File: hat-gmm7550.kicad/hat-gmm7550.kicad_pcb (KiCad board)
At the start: 4 copper layers, 65 x 56 mm, 83 parts, among them J1 VisionFive_GPIO, J10 Pmod 2x6, J2 Conn_01x02, J3 Conn_02x02_Odd_Even, J4 DNI, J5 DNI, J6 10144517-064802LF, J7 10144517-064802LF, J8 JTAG, J9 Pmod 2x6, Q1 NX6008NBK, Q2 NX6008NBK, Q3 NX6008NBK, Q4 FDC855N, U1 CAT24C32Y, U2 74LVC1G07, U3 ADM1177, U4 LSF0204PW, U5 LSF0204PW, U6 LSF0204PW, U7 LSF0204PW, U8 LSF0204PW, U9 LSF0204PW

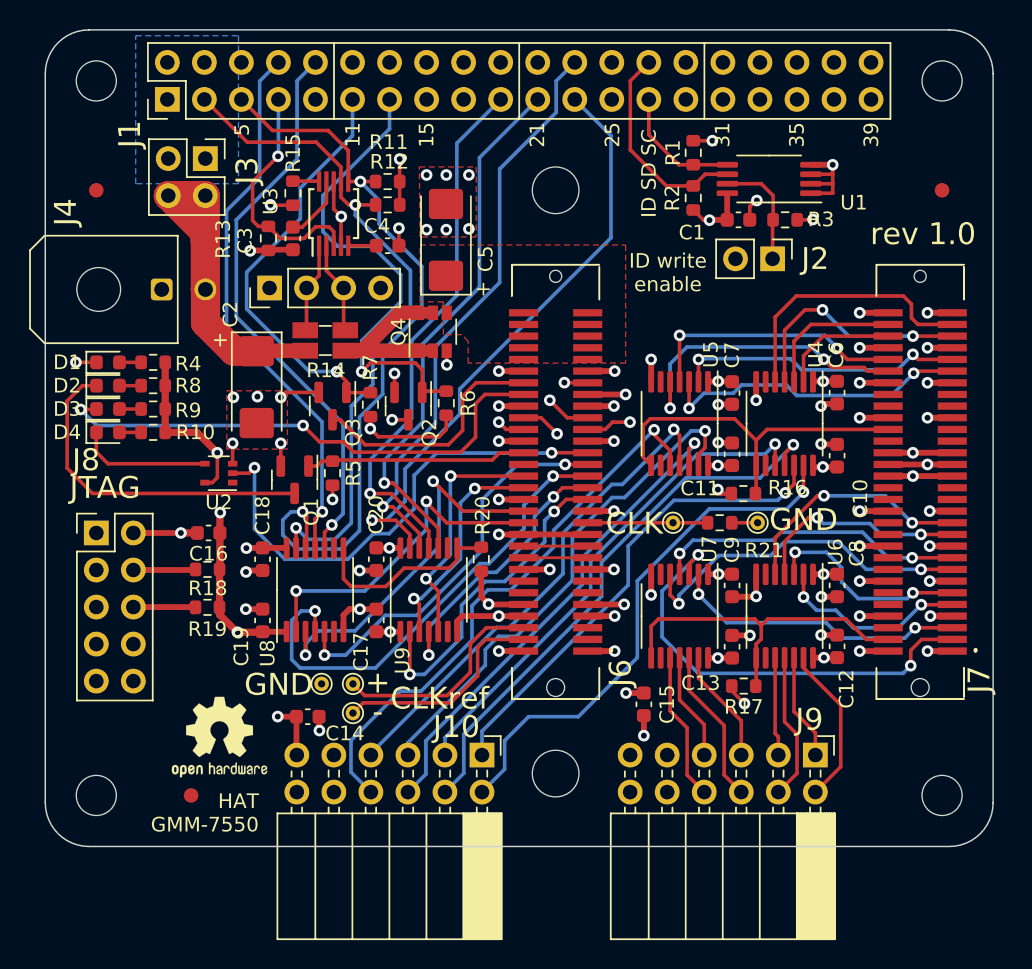
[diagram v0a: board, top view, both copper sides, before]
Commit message: Change U2 footprint due to the part availability, revision and date are updated (HAT GMM-7550)
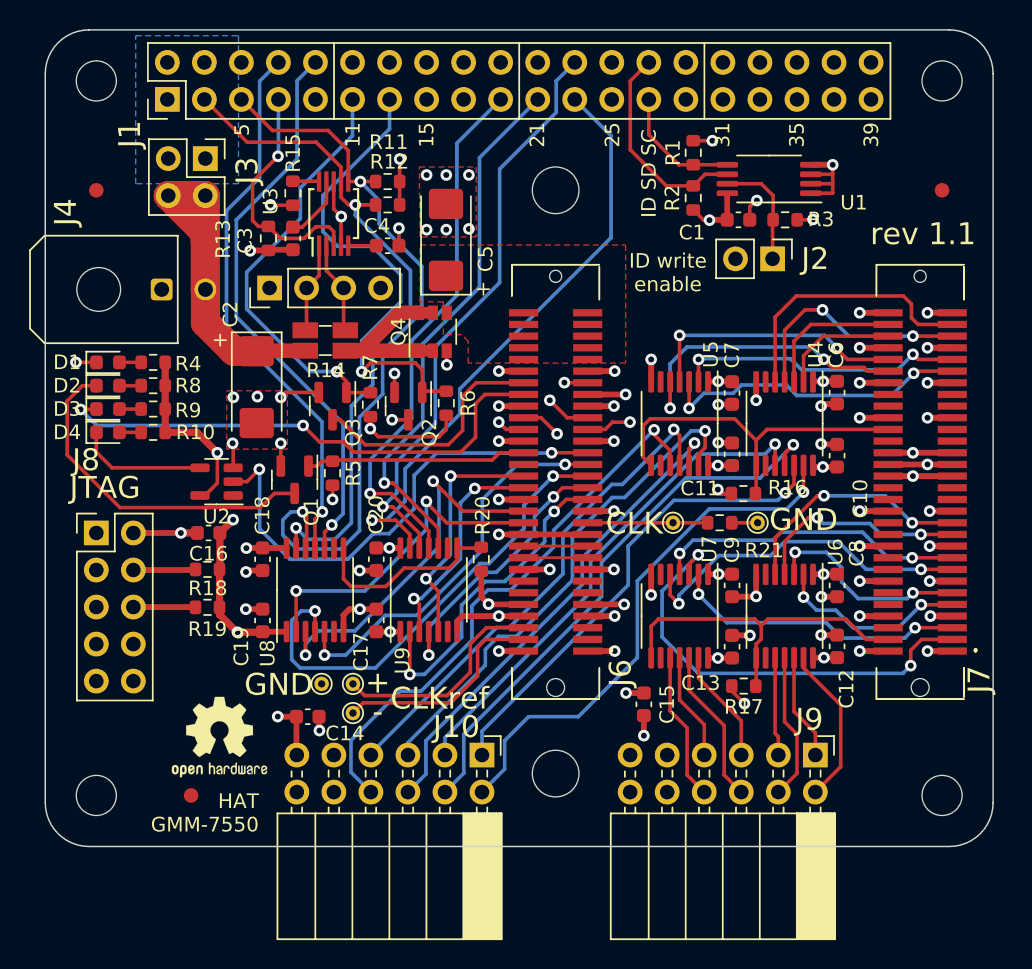
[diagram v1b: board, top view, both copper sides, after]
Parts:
- U2: footprint Package_TO_SOT_SMD:SOT-353_SC-70-5 -> Package_TO_SOT_SMD:SOT-23-5
- moved U2 0.60 mm to (81.8, 75.0)
- gave numbers to parts that had none: 4
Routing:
- net +2V5: track 138.9 -> 140.6 mm
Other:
- board text added: "rev 1.1"
- board text removed: "rev 1.0"
